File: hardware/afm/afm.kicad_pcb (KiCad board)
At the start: 2 copper layers, 100 x 100 mm, 179 parts, among them X1 USB-MINI-B, X2 BARREL_JACK, X3 CONN_01X06, X4 CONN_01X02, X5 PBD-20, X6 CONN_01X08

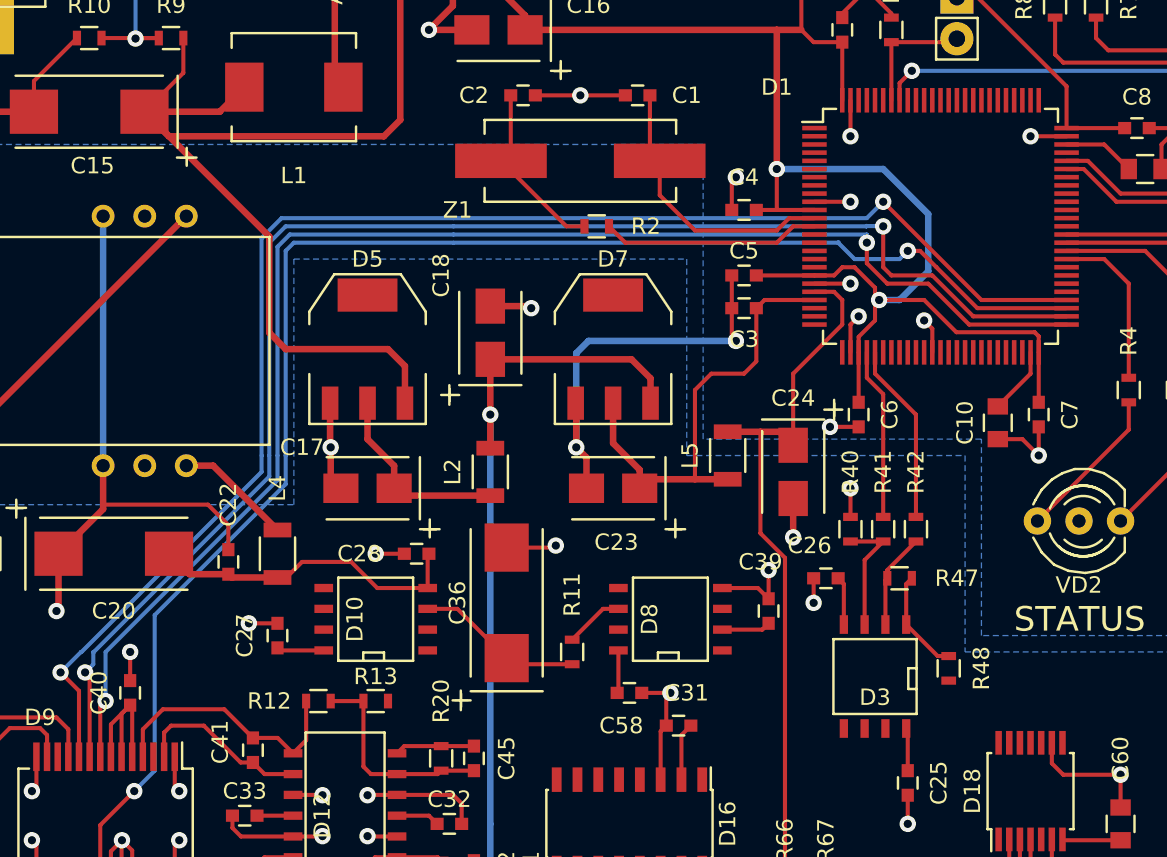
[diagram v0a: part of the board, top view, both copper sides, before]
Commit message: Piezo DAC moved from SPI2 to SPI3
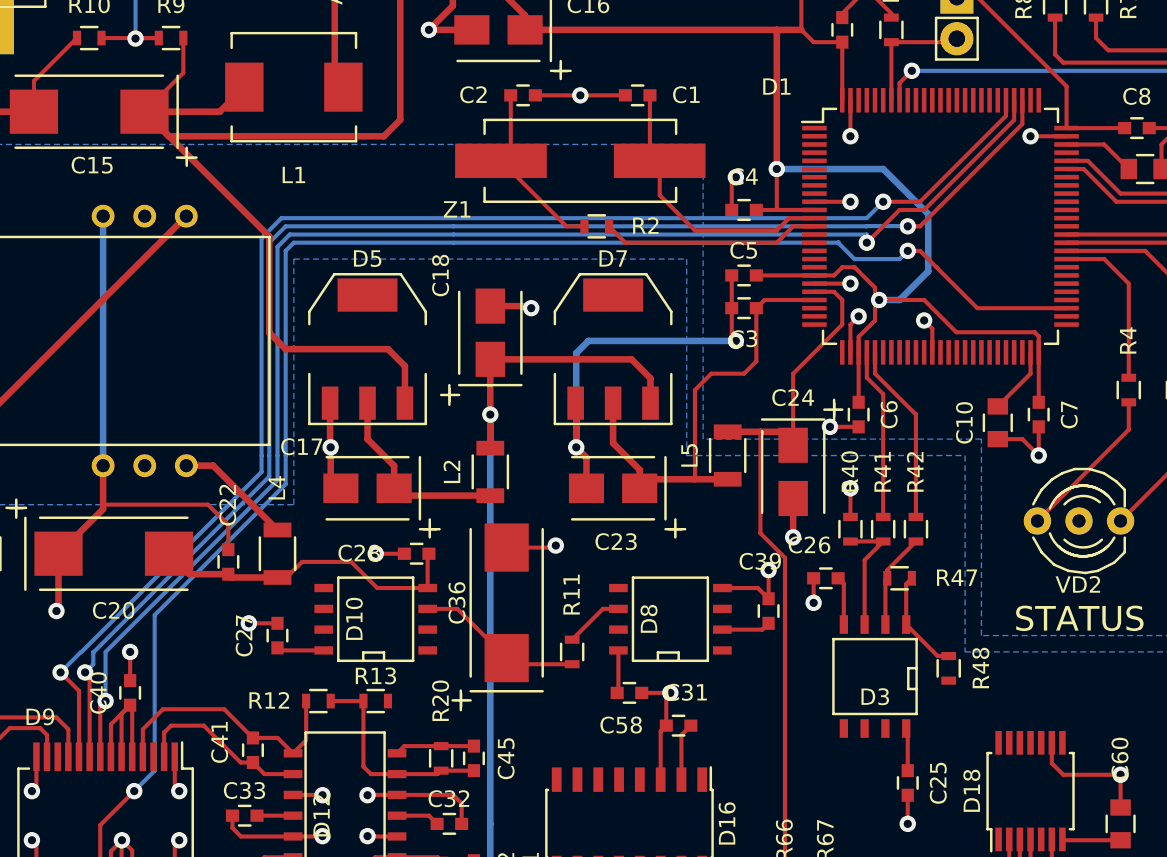
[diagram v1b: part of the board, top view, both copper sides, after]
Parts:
- Z1: value 25 MHz -> 8 MHz
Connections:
- D1 pad 51: PZ_CS -> Net-(D1-Pad51)
- D1 pad 52: PZ_CLK -> Net-(D1-Pad52)
- D1 pad 54: PZ_SDI -> Net-(D1-Pad54)
- D1 pad 78: Net-(D1-Pad78) -> PZ_CLK
- D1 pad 79: Net-(D1-Pad79) -> PZ_CS
- D1 pad 80: Net-(D1-Pad80) -> PZ_SDI
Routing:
- net PZ_SDI: track 89.8 -> 86.8 mm
- net PZ_CLK: track 89.1 -> 86.7 mm
- net PZ_CS: track 87.4 -> 85.8 mm

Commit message: PCB trace completed
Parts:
- moved R48 10.0 mm to (124.0, 97.0), turned to 0 degrees
- moved C65 1.25 mm to (116.8, 115.5)
- moved R65 1.25 mm to (116.8, 119.0)
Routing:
- net +15V: track 33.6 -> 260.1 mm, vias 0 -> 12
- net -15V: track 42.4 -> 238.2 mm, vias 0 -> 12
- net VCM_MUTE: track 0.00 -> 168.1 mm, vias 0 -> 6
- net OPU_ENA: track 0.00 -> 141.2 mm, vias 0 -> 2
- net VDD: track 135.2 -> 259.6 mm, vias 2 -> 7
- net Net-(D10-Pad1): track 0.00 -> 101.1 mm, vias 0 -> 6
- net CTL_SDI: track 0.00 -> 83.6 mm, vias 0 -> 3
- net ADC_BIAS: track 41.6 -> 120.1 mm, vias 0 -> 4
- net CTL_CLK: track 0.00 -> 76.7 mm, vias 0 -> 3
- net /Piezo drivers/ZMOD: track 0.00 -> 70.3 mm
- net CTL_VCM: track 0.00 -> 67.9 mm, vias 0 -> 2
- net STM_BIAS: track 4.88 -> 68.2 mm, vias 0 -> 2
- net +5V: track 114.2 -> 172.0 mm, vias 2 -> 4
- net /Piezo drivers/X: track 4.88 -> 62.0 mm, vias 0 -> 2
- net ADC_FOCUS: track 15.8 -> 71.8 mm, vias 0 -> 4
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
